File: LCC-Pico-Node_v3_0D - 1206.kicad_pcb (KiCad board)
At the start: 4 copper layers, 100 x 82 mm, 89 parts, among them IC1 TPS54228DR, IC2 MCP2518FD, IC3 MCP2562FD, IC5 256Kb, IC6 TPS54228DR, J1 RJ45, J12 Power Sel, J15 Analog I/O, J16 NVM Power Sel, J2 RJ45, J20 Barrel Jack, J21 I/O - 1, J24 Ext. Reset, J27 MasterPower, J3 LCC Pwr Sel, J4 I/O - 2, J5 External Power, J6 Power Sel, J7 External Power, Q1 DMG2305UX-7, SW1 button, SW2 button, SW3 button, Y1 ABM-40MHZ

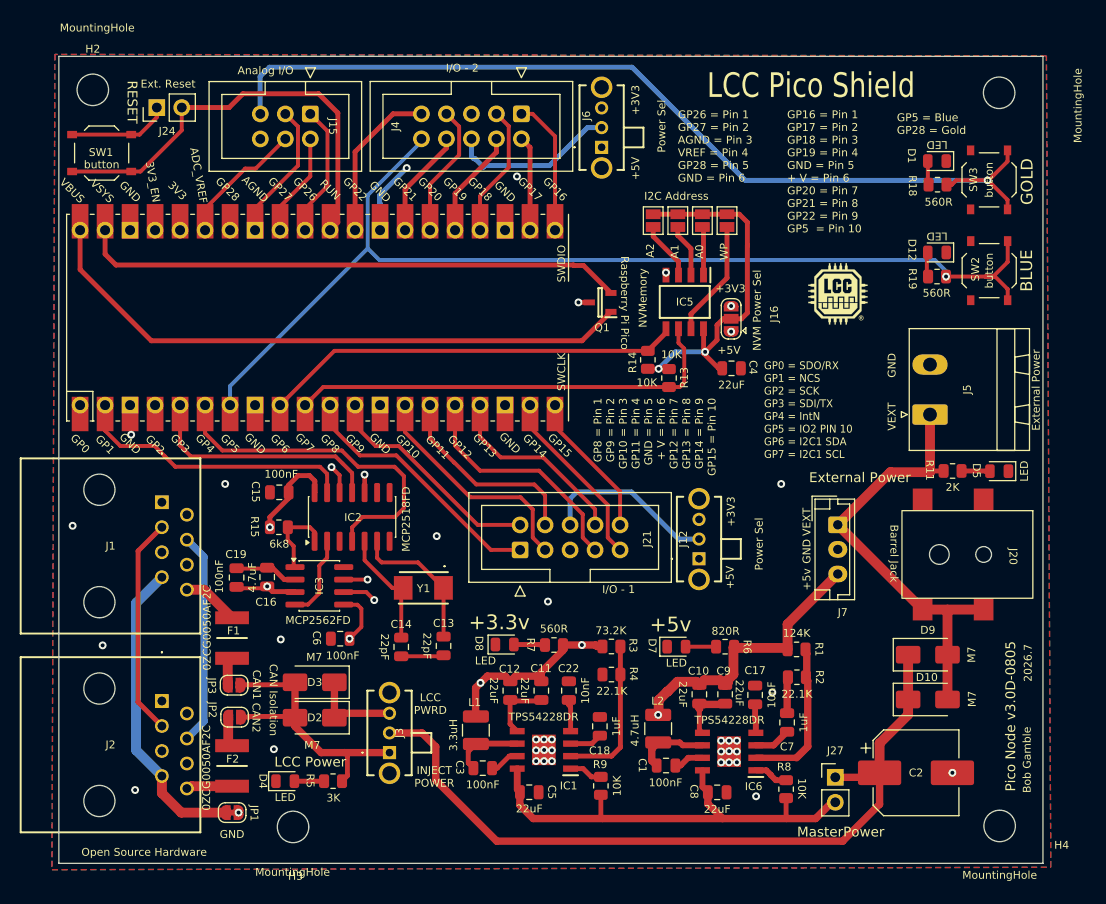
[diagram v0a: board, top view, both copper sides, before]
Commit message: Screen print cleanup
minor updates and formatting of screen print content
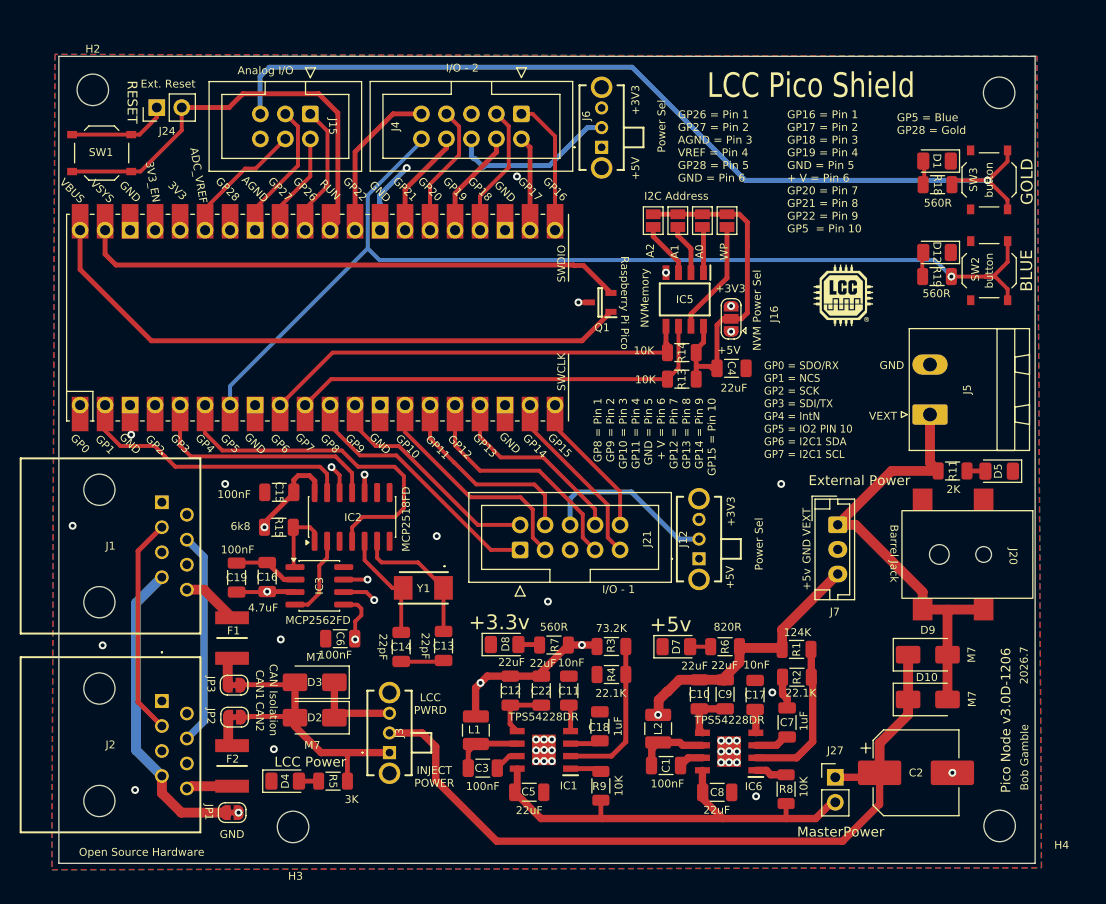
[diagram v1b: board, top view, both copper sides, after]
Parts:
- C1, C10, C11, C12, C13, C14, C15, C16, C17, C18, C19, C22, C3, C4, C5, C6, C7, C8, C9: footprint Capacitor_SMD:C_0805_2012Metric -> Capacitor_SMD:C_1206_3216Metric
- D1, D12, D4, D5, D7, D8: footprint LED_SMD:LED_0805_2012Metric -> LED_SMD:LED_1206_3216Metric
- F1, F2: value 0ZCG0050AF2C -> 0ZCG0035AF2C
- IC5: value 256Kb -> MB85RCxxxV
- JP2, JP3: footprint Jumper:SolderJumper-2_P1.3mm_Open_RoundedPad1.0x1.5mm -> Jumper:SolderJumper-2_P1.3mm_Bridged_RoundedPad1.0x1.5mm
- R1, R11, R13, R14, R15, R18, R19, R2, R3, R4, R5, R6, R7, R8, R9: footprint Resistor_SMD:R_0805_2012Metric -> Resistor_SMD:R_1206_3216Metric
- moved R14 3.53 mm to (163.7, 82.7), turned to 0 degrees
- moved REF** 2.01 mm to (178.2, 80.7)
- moved REF** 1.86 mm to (188.3, 80.7)
- moved R13 1.31 mm to (163.7, 85.4), turned to 0 degrees
- moved G*** 1.08 mm to (157.1, 70.2)
- moved G*** 0.57 mm to (180.2, 76.8)
- moved IC5 0.25 mm to (164.0, 77.3)
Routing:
- net Net-(IC5-VDD): track 39.0 -> 35.5 mm, vias 2 -> 0
- net +5V: track 178.2 -> 174.9 mm
- net +3V3: track 169.1 -> 167.0 mm
- net SCL1: track 45.4 -> 43.8 mm
- net Net-(D8-A): track 3.73 -> 2.17 mm
- net Net-(D5-A): track 3.35 -> 1.88 mm
- net SDA1: track 42.9 -> 44.3 mm
- net GND: track 44.9 -> 43.5 mm
- net VINPUT: track 47.7 -> 46.3 mm
- net Net-(D7-A): track 3.10 -> 2.09 mm
- net Net-(D4-A): track 3.01 -> 2.00 mm
- net /TXD: track 8.23 -> 7.43 mm
- net VEXT: track 46.5 -> 47.1 mm
- net GP28: track 108.9 -> 108.3 mm
- net Net-(IC6-SS): track 2.93 -> 2.41 mm
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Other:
- board size 100 x 82 mm -> 99.2 x 82 mm
- board text added: "Pico Node v3.0D-1206"
- board text removed: "Pico Node v3.0D-0805"
